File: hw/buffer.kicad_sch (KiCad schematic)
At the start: 27 parts, among them J3 BNC, K2 G6S-2, U14 AQY225R2S, U18 TS5A63157DBV, U19 OPA859xDSG, U20 AD8370

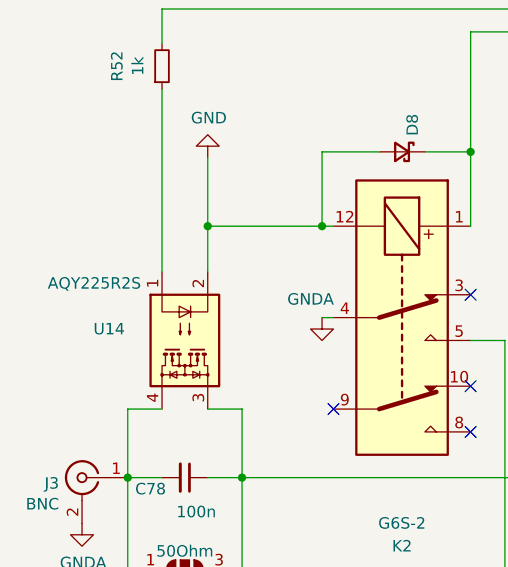
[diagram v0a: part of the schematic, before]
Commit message: V3 component modifications
- SS relay is AQY280S (cheaper than original component; should do it)
- PGA serial interface translator resistors 10k->5k1

  Had erroneously populated with 18k which did not work (unclear why);
  after dropping to 5k1 it works fine.
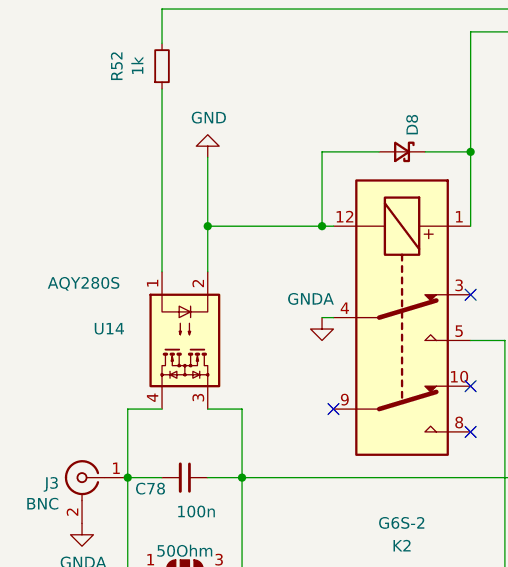
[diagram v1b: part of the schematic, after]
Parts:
- U14: value AQY225R2S -> AQY280S
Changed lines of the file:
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@@
       (effects (font (size 1.27 1.27)) (justify right))
     )
-    (property "Value" "AQY225R2S" (at 50.8 80.01 90)
+    (property "Value" "AQY280S" (at 50.8 80.01 90)
       (effects (font (size 1.27 1.27)) (justify right))
     )

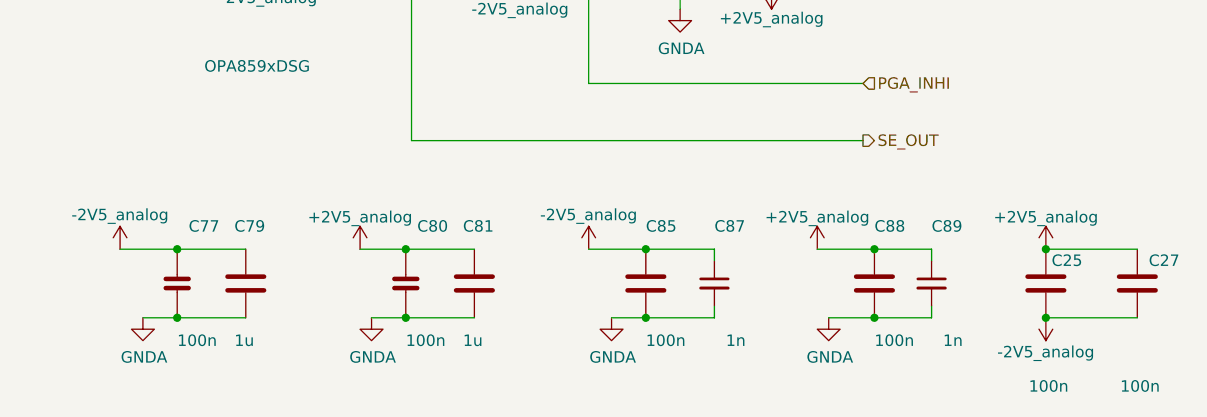
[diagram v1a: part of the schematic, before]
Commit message: consolidated components to simplify BOM
(nothing actually changed but the symbols representing identical
components are now identical -> no more multiple BOM entries for
the same type of component).
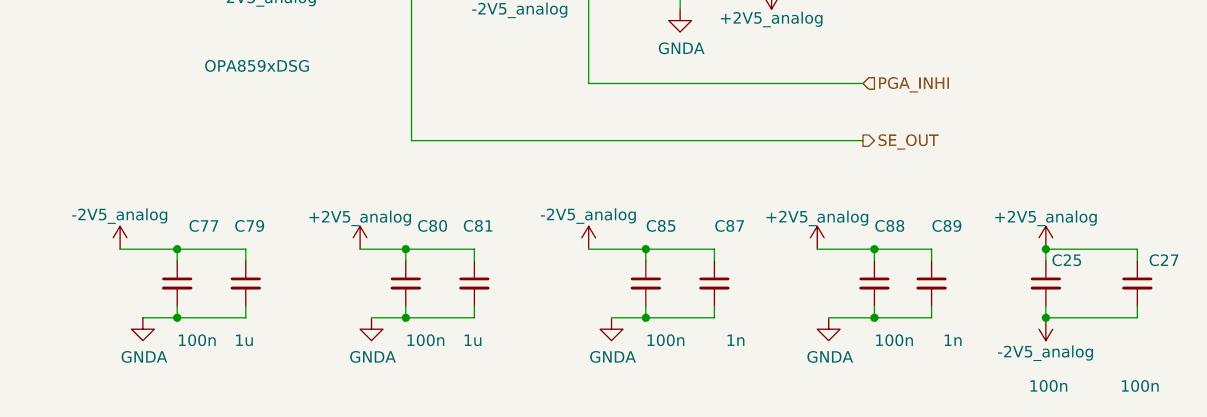
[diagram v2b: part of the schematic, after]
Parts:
- C25, C27, C85, C88: symbol fmc:100nF_603 -> Device:C_Small; Manufacturer (none) -> Samsung; Part (none) -> CL10B104KB8NFN
- C77, C80: symbol fmc:100nF_402 -> Device:C_Small; Manufacturer (none) -> Samsung; Part (none) -> CL10B104KB8NFN
- C79, C81: symbol fmc:1uF_805 -> Device:C_Small; Manufacturer (none) -> TDK; Part (none) -> CGA4J2X7R1C105K125AA
- C82: Manufacturer (none) -> Samsung; Part (none) -> CL10B104KB8NFN

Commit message: consolidated 1n caps -> use 2n everywhere
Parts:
- C87, C89, C90: value 1n -> 2n
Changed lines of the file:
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@@
       (effects (font (size 1.27 1.27)) (justify left))
     )
-    (property "Value" "1n" (at 215.9 114.3 0)
+    (property "Value" "2n" (at 215.9 114.3 0)
       (effects (font (size 1.27 1.27)) (justify left))
     )
@@
       (effects (font (size 1.27 1.27)) (justify left))
     )
-    (property "Value" "1n" (at 218.44 154.94 0)
+    (property "Value" "2n" (at 218.44 154.94 0)
       (effects (font (size 1.27 1.27)) (justify left))
     )
@@
       (effects (font (size 1.27 1.27)) (justify left))
     )
-    (property "Value" "1n" (at 242.57 154.94 0)
-      (effects (font (size 1.27 1.27)) (justify left))
-    )
+    (property "Value" "2n" (at 242.57 154.94 0)
+      (effects (font (size 1.27 1.27)) (justify left))
+    )

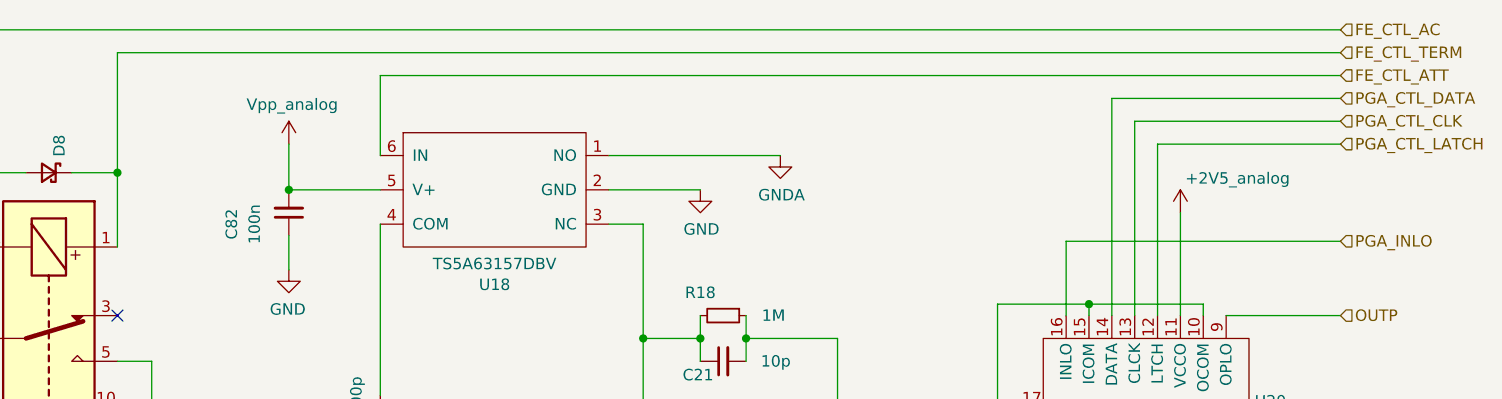
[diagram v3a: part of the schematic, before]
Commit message: added pull-downs to ctl-input of analog-switches (U11, U18).
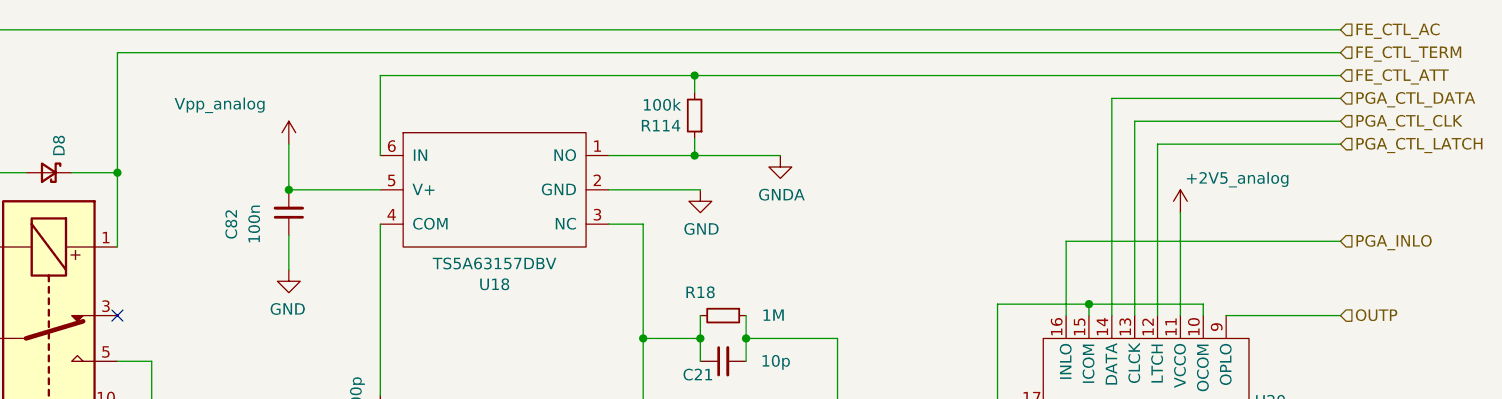
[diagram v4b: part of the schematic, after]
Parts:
- added R114: 100k, Resistor_SMD:R_0603_1608Metric, symbol Device:R_Small
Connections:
- net FE_CTL_ATT: now also R114.2
- net GNDA: now also R114.1
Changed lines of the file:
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@@
   (junction (at 72.39 101.6) (diameter 0) (color 0 0 0 0)
   )
+  (junction (at 161.925 63.5) (diameter 0) (color 0 0 0 0)
+  )
   (junction (at 234.95 144.78) (diameter 0) (color 0 0 0 0)
   )
@@
   )
   (junction (at 156.21 101.6) (diameter 0) (color 0 0 0 0)
+  )
+  (junction (at 161.925 54.61) (diameter 0) (color 0 0 0 0)
   )
   (junction (at 167.64 96.52) (diameter 0) (color 0 0 0 0)
@@
   (no_connect (at 97.79 96.52))
   (no_connect (at 97.79 81.28))
-  (wire (pts (xy 152.4 63.5) (xy 171.45 63.5))
+  (wire (pts (xy 152.4 63.5) (xy 161.925 63.5))
     (stroke (width 0) (type default))
   )
@@
     (stroke (width 0) (type default))
   )
+  (wire (pts (xy 161.925 61.595) (xy 161.925 63.5))
+    (stroke (width 0) (type default))
+  )
   (wire (pts (xy 81.28 65.405) (xy 87.63 65.405))
     (stroke (width 0) (type default))
@@
     (stroke (width 0) (type default))
   )
+  (wire (pts (xy 161.925 63.5) (xy 171.45 63.5))
+    (stroke (width 0) (type default))
+  )
   (wire (pts (xy 182.88 144.78) (xy 190.5 144.78))
     (stroke (width 0) (type default))
@@
     (stroke (width 0) (type default))
   )
+  (wire (pts (xy 161.925 54.61) (xy 233.68 54.61))
+    (stroke (width 0) (type default))
+  )
   (wire (pts (xy 177.8 144.78) (xy 182.88 144.78))
     (stroke (width 0) (type default))
@@
     (stroke (width 0) (type default))
   )
-  (wire (pts (xy 127 54.61) (xy 233.68 54.61))
+  (wire (pts (xy 127 54.61) (xy 161.925 54.61))
     (stroke (width 0) (type default))
   )
@@
   )
   (wire (pts (xy 152.4 67.31) (xy 162.56 67.31))
+    (stroke (width 0) (type default))
+  )
+  (wire (pts (xy 161.925 54.61) (xy 161.925 56.515))
     (stroke (width 0) (type default))
   )
@@
       (effects (font (size 1.27 1.27)) hide)
     )
-    (property "Value" "Vpp_analog" (at 117.221 57.8358 0)
+    (property "Value" "Vpp_analog" (at 109.22 57.785 0)
       (effects (font (size 1.27 1.27)))
     )
@@
         )
       )
+    )
+  )
+  (symbol (lib_id "Device:R_Small") (at 161.925 59.055 180) (unit 1)
+    (in_bom yes) (on_board yes) (dnp no)
+    (property "Reference" "R114" (at 160.4264 60.2234 0)
+      (effects (font (size 1.27 1.27)) (justify left))
+    )
+    (property "Value" "100k" (at 160.4264 57.912 0)
+      (effects (font (size 1.27 1.27)) (justify left))
+    )
+    (property "Footprint" "Resistor_SMD:R_0603_1608Metric" (at 161.925 59.055 0)
+      (effects (font (size 1.27 1.27)) hide)
+    )
+    (property "Datasheet" "~" (at 161.925 59.055 0)
+      (effects (font (size 1.27 1.27)) hide)
+    )
+    (pin "1")
+    (pin "2")
+    (instances
+      (project "usbadc"
+        (path "/7c8a1f8d-8834-4c9b-aaae-1f231e9b09a1/c969de1a-32a7-4770-b1aa-e527a627ef90/2d0efa78-153a-4cb7-91b5-dea78ecb841c"
+          (reference "R114") (unit 1)
+        )
+        (path "/7c8a1f8d-8834-4c9b-aaae-1f231e9b09a1/c969de1a-32a7-4770-b1aa-e527a627ef90/48d00771-072a-4471-832b-aaf429246191"
+          (reference "R115") (unit 1)
+        )
+      )

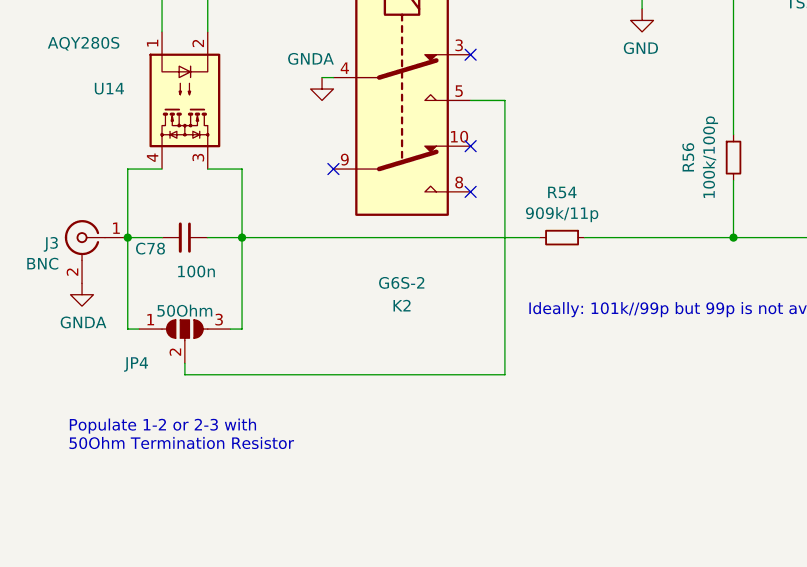
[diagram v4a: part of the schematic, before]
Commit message: [hw]: updated relay part no.
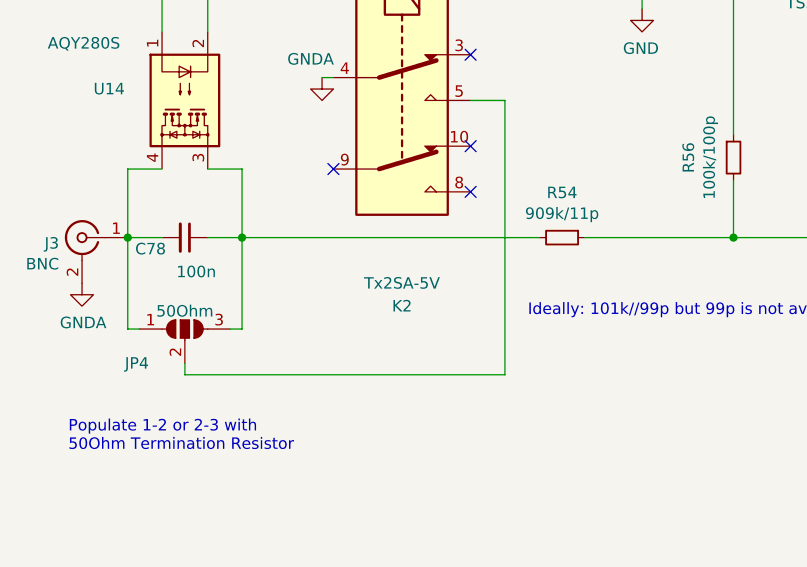
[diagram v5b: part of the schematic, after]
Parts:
- K2: value G6S-2 -> Tx2SA-5V
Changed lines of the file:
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@@
       (effects (font (size 1.27 1.27)))
     )
-    (property "Value" "G6S-2" (at 90.17 106.68 90)
+    (property "Value" "Tx2SA-5V" (at 90.17 106.68 90)
       (effects (font (size 1.27 1.27)))
     )
@@
       (effects (font (size 1.27 1.27)) (justify left) hide)
     )
-    (property "Datasheet" "http://omronfs.omron.com/en_US/ecb/products/pdf/en-g6s.pdf" (at 90.17 83.82 0)
+    (property "Datasheet" "" (at 90.17 83.82 0)
       (effects (font (size 1.27 1.27)) hide)
     )

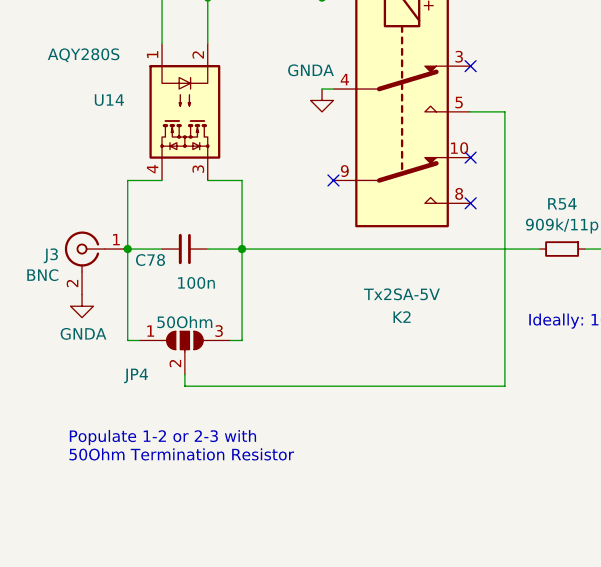
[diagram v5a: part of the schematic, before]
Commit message: [hw]: changed input AC-coupling cap from 100n->10n
Does not affect PCB
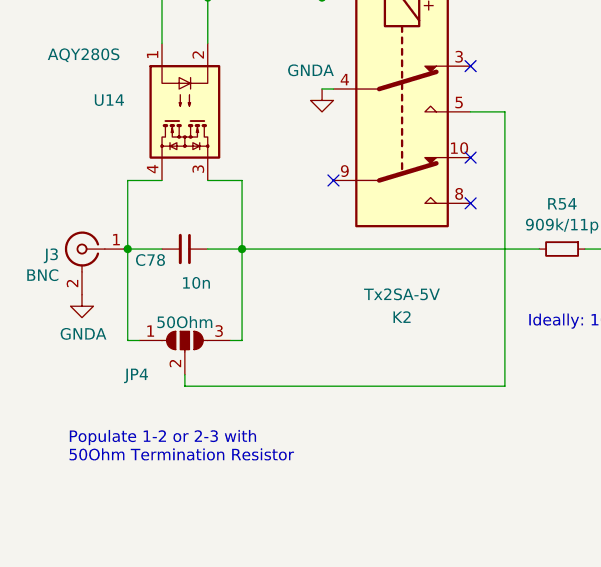
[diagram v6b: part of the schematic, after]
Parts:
- C78: value 100n -> 10n
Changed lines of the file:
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@@
       (effects (font (size 1.27 1.27)))
     )
-    (property "Value" "100n" (at 67.31 105.41 90)
+    (property "Value" "10n" (at 67.31 105.41 90)
       (effects (font (size 1.27 1.27)))
     )

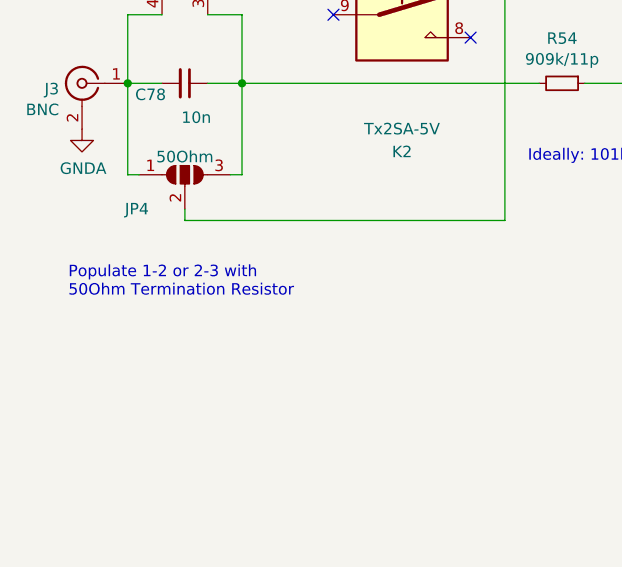
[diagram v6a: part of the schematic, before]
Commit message: renaming, comments, part/vendor and other cosmetics (no pcb change)
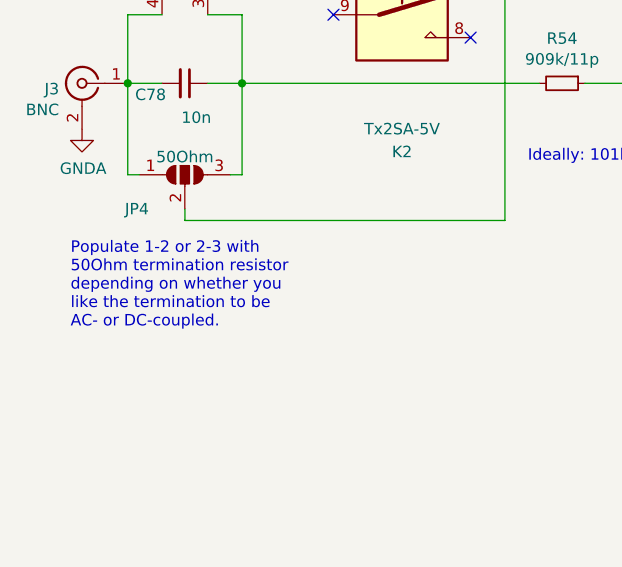
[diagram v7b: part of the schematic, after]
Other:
- note added: "Populate 1-2 or 2-3 with 50Ohm termination resistor depending on whether you like the termination to be AC- or DC-coupled."
- note removed: "Populate 1-2 or 2-3 with 50Ohm Termination Resistor"
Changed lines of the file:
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@@
     (effects (font (size 1.27 1.27)) (justify left bottom))
   )
-  (text "Populate 1-2 or 2-3 with\n50Ohm Termination Resistor"
-    (at 53.086 125.476 0)
+  (text "Populate 1-2 or 2-3 with\n50Ohm termination resistor\ndepending on whether you\nlike the termination to be\nAC- or DC-coupled."
+    (at 53.34 128.905 0)
     (effects (font (size 1.27 1.27)) (justify left bottom))
   )
